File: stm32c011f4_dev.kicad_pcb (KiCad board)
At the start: 2 copper layers, 38.5 x 32 mm, 25 parts, among them J3 Conn_01x14_Pin, J5 Conn_01x14_Pin, P1 USB_C_Plug_USB2.0, SW3 SW_Push, SW4 SW_Push, U2 STM32G030K6Tx, U3 DI78L3.3UAB-DIO, Y1 LFXTAL069528CUTT

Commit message: Silkscreen update
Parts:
- moved REF** 18.5 mm to (53.5, 44.0)
- moved C3 0.50 mm to (32.0, 28.5)
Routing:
- net Earth: track 85.1 -> 98.2 mm, vias 10 -> 11
- net PB0: track 26.9 -> 27.6 mm
- net Net-(D3-A): track 9.56 -> 8.98 mm
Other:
- board text added: "3v3"
- board text added: "GND"
- board text added: "PA0"
- board text added: "PA1"
- board text added: "PA11"
- board text added: "PA12"
- board text added: "PA13"
- board text added: "PA15"
- board text added: "PA2"
- board text added: "PA3"
- board text added: "PA4"
- board text added: "PA5"
- board text added: "PA6"
- board text added: "PA7"
- board text added: "PA8"
- board text added: "PB0"
- board text added: "PB1"
- board text added: "PB2"
- board text added: "PB3"
- board text added: "PB4"
- board text added: "PB5"
- board text added: "PB6"
- board text added: "PB7"
- board text added: "PB8"
- board text added: "PB9"
- board text added: "PC6"
- board text added: "VIN"

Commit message: pcb update
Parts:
- moved SW4 0.10 mm to (24.0, 45.5)
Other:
- board size 38.5 x 32 mm -> 39 x 32 mm
- board text added: "RX"
- board text added: "TX"
- board text removed: "${REFERENCE}"
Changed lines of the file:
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@@
 	(footprint "Button_Switch_SMD:SW_SPST_EVQQ2"
 		(layer "F.Cu")
-		(at 23.9 45.5)
+		(at 24 45.5)
 		(descr "Light Touch Switch, https://industrial.panasonic.com/cdbs/www-data/pdf/ATK0000/ATK0000CE28.pdf")
 		(property "Reference" "SW4"
@@
 		(tags "LED")
 		(property "Reference" "D1"
-			(at 0 -1.43 180)
+			(at 2.2125 0 180)
 			(layer "F.SilkS")
 			(effects
@@
 		(tags "Through hole pin header THT 1x14 2.54mm single row")
 		(property "Reference" "J5"
-			(at 0 -2.33 -90)
+			(at 2 -0.84 180)
 			(layer "F.SilkS")
 			(effects
@@
 		(tags "Through hole pin header THT 1x14 2.54mm single row")
 		(property "Reference" "J3"
-			(at 0 -2.33 -90)
+			(at -2 -0.96 180)
 			(layer "F.SilkS")
 			(effects
@@
 		(tags "resistor")
 		(property "Reference" "R8"
-			(at 0 -1.43 0)
+			(at 1.7875 -1.35625 0)
 			(layer "F.SilkS")
+			(hide yes)
 			(effects
 				(font
@@
 		(tags "SMD SMT crystal")
 		(property "Reference" "Y1"
-			(at 0 -2 180)
+			(at 1.1 -2.3 180)
 			(layer "F.SilkS")
 			(effects
@@
 	)
 	(gr_rect
-		(start 18.5 20.5)
+		(start 18 20.5)
 		(end 57 52.5)
 		(stroke
@@
 		)
 	)
-	(gr_text "made by Lorbasta"
-		(at 56.5 41 90)
+	(gr_text "RX"
+		(at 46 49 0)
+		(layer "F.SilkS")
+		(effects
+			(font
+				(size 1 1)
+				(thickness 0.25)
+				(bold yes)
+			)
+			(justify left bottom)
+		)
+	)
+	(gr_text "TX"
+		(at 46 45.5 0)
 		(layer "F.SilkS")
 		(effects
@@
 		)
 	)
-	(gr_text "${REFERENCE}"
-		(at 33 38 0)
-		(layer "F.Fab")
+	(gr_text "made by Lorbasta"
+		(at 56.5 41 90)
+		(layer "F.SilkS")
 		(effects
 			(font
-				(size 0.4 0.4)
-				(thickness 0.06)
+				(size 1 1)
+				(thickness 0.25)
+				(bold yes)
 			)
+			(justify left bottom)
 		)
 	)

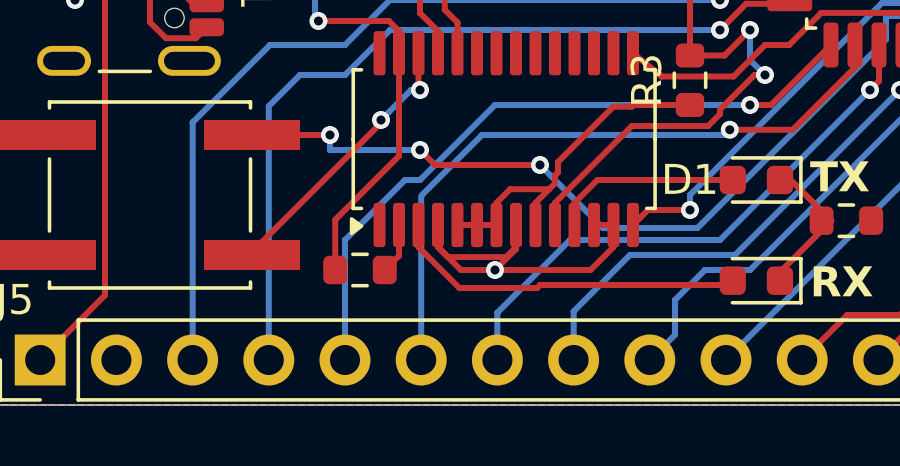
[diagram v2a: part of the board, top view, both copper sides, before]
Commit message: pcb update
fixed gnd mistakes
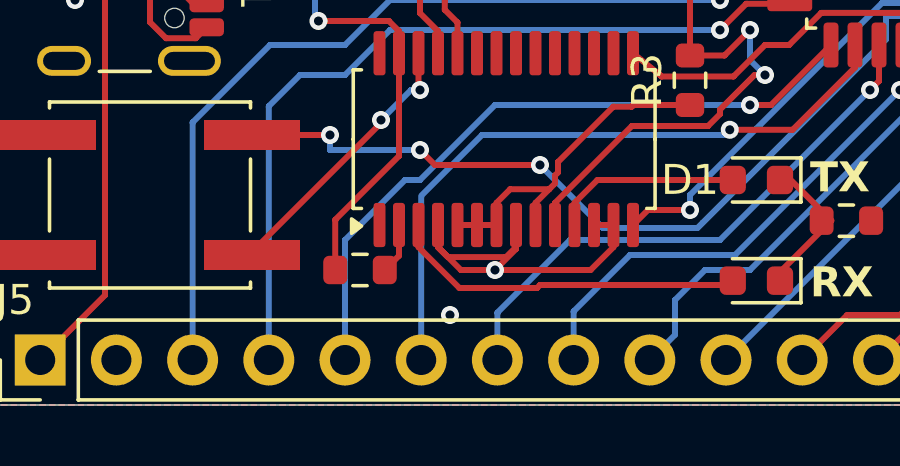
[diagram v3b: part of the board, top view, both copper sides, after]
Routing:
- net Earth: vias 11 -> 12
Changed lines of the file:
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@@
 			(layer "F.Fab")
 		)
-		(fp_text user "${REFERENCE}"
-			(at -12.5125 -15.35625 0)
-			(layer "F.Fab")
-			(effects
-				(font
-					(size 1 1)
-					(thickness 0.15)
-				)
-			)
-		)
 		(pad "1" smd roundrect
 			(at -1.65 0 180)
@@
 		(size 0.6)
 		(drill 0.3)
+		(layers "F.Cu" "B.Cu")
+		(free yes)
+		(net 2)
+	)
+	(via
+		(at 34 49.5)
+		(size 0.6)
+		(drill 0.3)

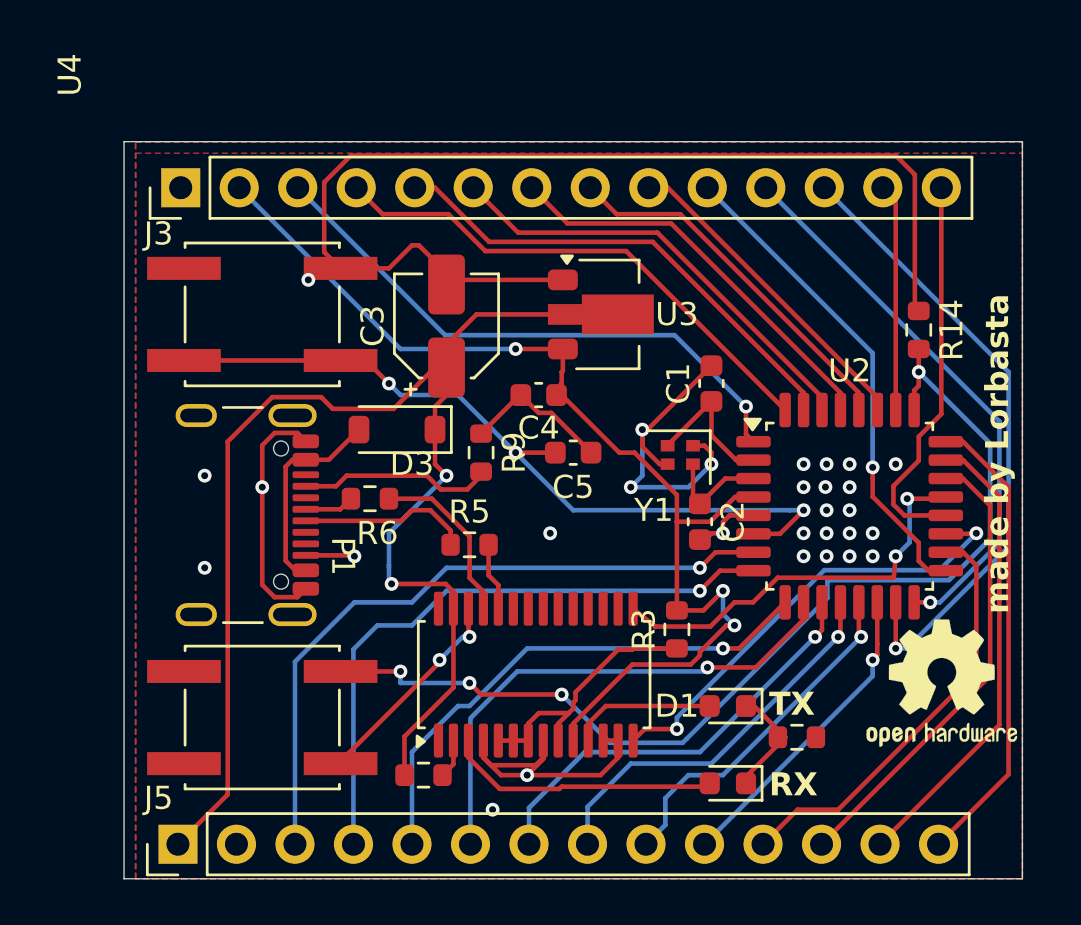
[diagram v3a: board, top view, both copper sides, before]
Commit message: PCB update
adding swd and improving traces
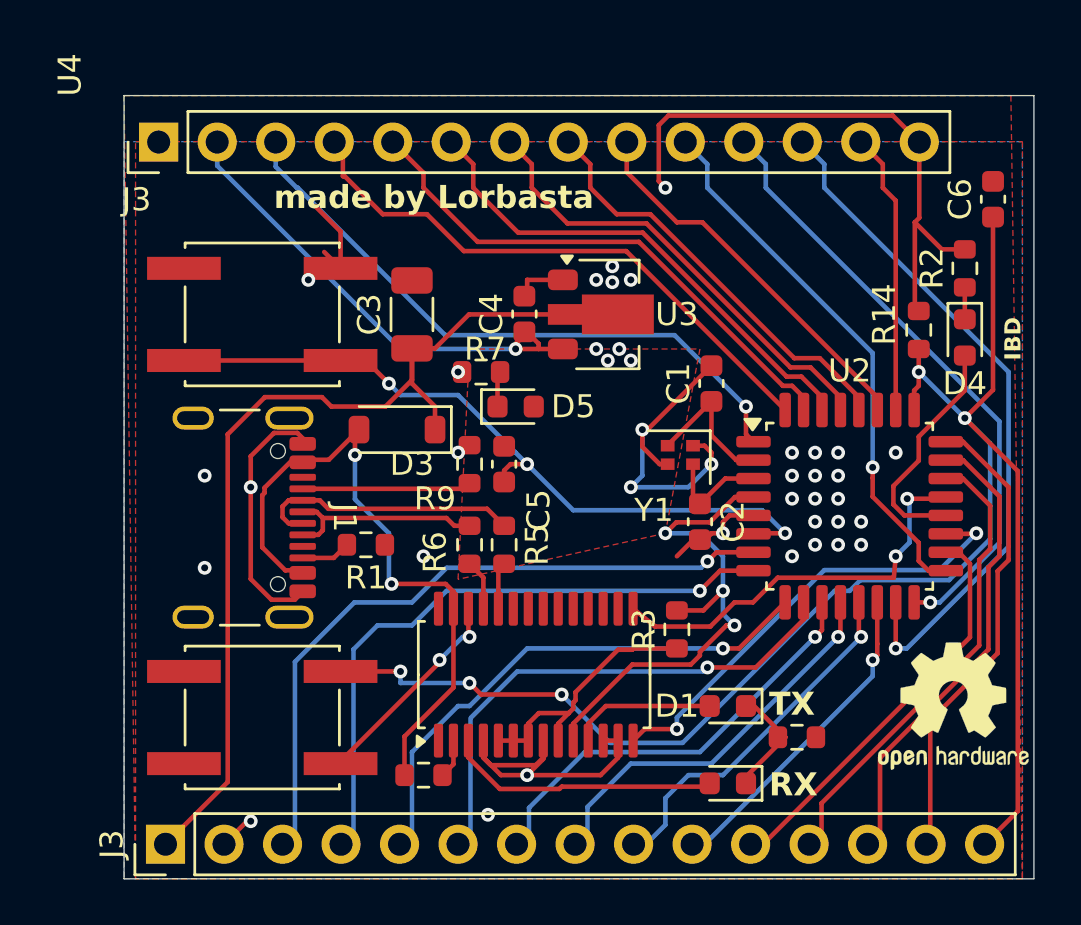
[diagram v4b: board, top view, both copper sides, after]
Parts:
- removed J5: Conn_01x14_Pin, Connector_PinHeader_2.54mm:PinHeader_1x14_P2.54mm_Vertical
- removed P1: USB_C_Plug_USB2.0, Connector_USB:USB_C_Receptacle_GCT_USB4105-xx-A_16P_TopMnt_Horizontal
- added C6: 100nF, Capacitor_SMD:C_0603_1608Metric, F.Cu at (55.7, 23.0)
- added D4: LED, LED_SMD:LED_0603_1608Metric, F.Cu at (54.5, 29.0)
- added D5: LED, LED_SMD:LED_0603_1608Metric, F.Cu at (35.0, 32.0)
- added J1: USB_C_Receptacle_USB2.0_16P, Connector_USB:USB_C_Receptacle_GCT_USB4105-xx-A_16P_TopMnt_Horizontal, F.Cu at (22.1, 36.8)
- added J3: Conn_01x15_Pin, Connector_PinHeader_2.54mm:PinHeader_1x15_P2.54mm_Vertical, F.Cu at (19.8, 51.0)
- added R1: 5k, Resistor_SMD:R_0603_1608Metric, F.Cu at (28.5, 38.0)
- added R2: 220, Resistor_SMD:R_0603_1608Metric, F.Cu at (54.5, 26.0)
- added R7: 220, Resistor_SMD:R_0603_1608Metric, F.Cu at (33.5, 30.5)
- C3: value 1uF -> 10uF; footprint Capacitor_SMD:CP_Elec_4x5.3 -> Capacitor_SMD:C_1206_3216Metric
- R9: value 56k -> 5k
- moved R6 4.77 mm to (33.0, 38.0), turned to -90 degrees
- moved C4 3.57 mm to (35.4, 28.0), turned to 90 degrees
- moved C5 3.04 mm to (34.5, 34.5), turned to 90 degrees
- moved J3 2.20 mm to (19.5, 20.5)
- moved C3 1.58 mm to (30.5, 28.0)
- moved R5 1.50 mm to (34.5, 38.0), turned to -90 degrees
- moved REF** 1.12 mm to (54.0, 45.0)
- moved R9 0.71 mm to (33.0, 34.5)
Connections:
- C3 pad 1: VBUS -> VIN
- D3 pad 1: VBUS -> VIN
- D3 pad 2: Net-(D3-A) -> VBUS
- J3 pad 14: PC6 -> Earth
- U2 pad 20: PC6 -> Net-(D4-A)
- U3 pad 2: VBUS -> VIN
- Y1 pad 2: OSC_IN -> Earth
- Y1 pad 4: Earth -> OSC_OUT
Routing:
- net VIN: track 0.00 -> 40.3 mm
- net VBUS: track 58.8 -> 28.9 mm
- net Net-(J3-Pin_15): track 44.9 -> 73.8 mm, vias 4 -> 5
- net Earth: track 98.2 -> 77.6 mm, vias 12 -> 40
- net PC6: track 17.1 -> 0.00 mm
- net Net-(D4-A): track 0.00 -> 10.2 mm
- net Net-(D3-A): track 8.98 -> 0.00 mm
- net DP: track 2.15 -> 8.99 mm
- net Net-(U4-DP): track 7.56 -> 2.20 mm
- net 3v3: track 49.2 -> 43.9 mm, vias 3 -> 4
- net DM: track 7.71 -> 11.6 mm
- net PB3: track 14.2 -> 16.8 mm
- net PB8: track 22.6 -> 25.0 mm
- net PB9: track 25.1 -> 27.5 mm
- net PB6: track 19.5 -> 21.8 mm
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- added copper zone on F.Cu, net 3v3
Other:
- board size 39 x 32 mm -> 39.5 x 34 mm
- board text added: "CLK"
- board text added: "IBD"
- board text removed: "PC6"

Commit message: Changing usb-c from smt to tht
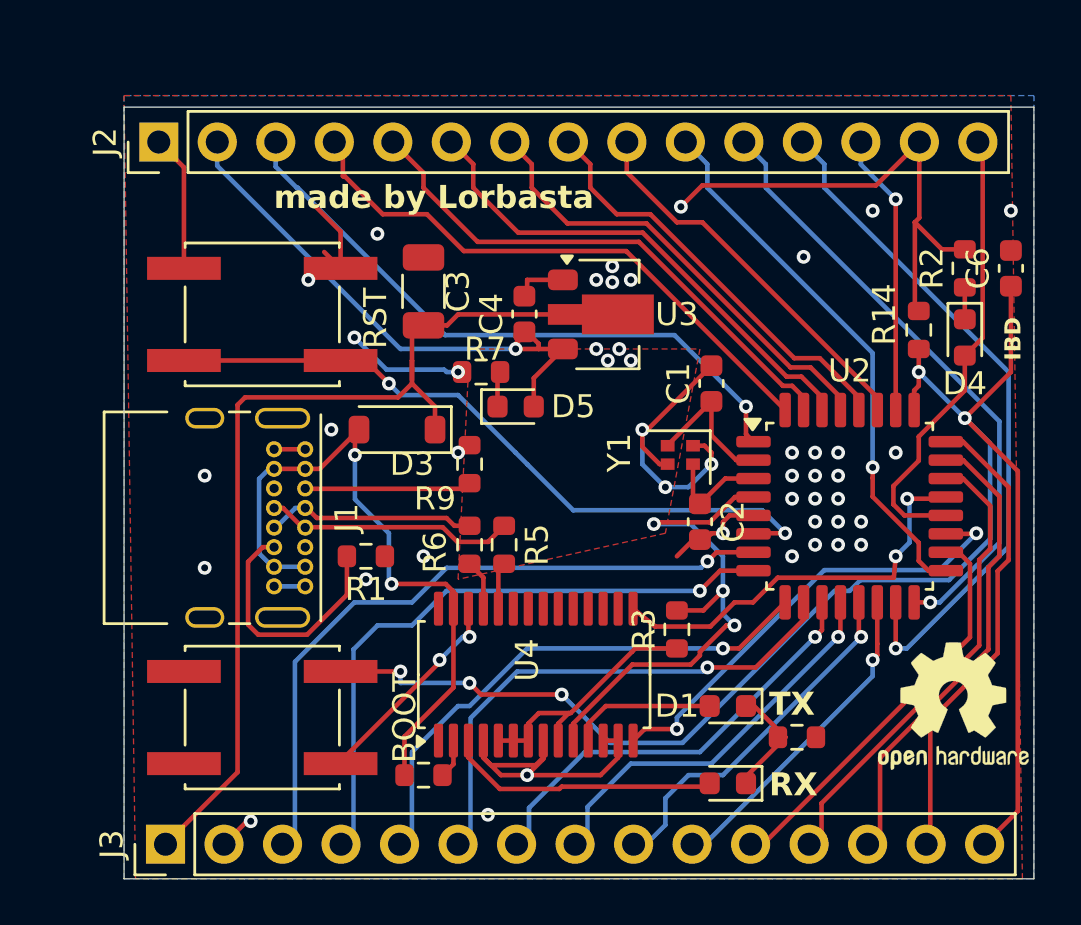
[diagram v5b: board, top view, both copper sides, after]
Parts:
- removed C5: 100nF, Capacitor_SMD:C_0603_1608Metric
- removed the J3 at (19.5, 20.5)
- added J2: Conn_01x15_Pin, Connector_PinHeader_2.54mm:PinHeader_1x15_P2.54mm_Vertical, F.Cu at (19.5, 20.5)
- J1: footprint Connector_USB:USB_C_Receptacle_GCT_USB4105-xx-A_16P_TopMnt_Horizontal -> Connector_USB:USB_C_Receptacle_GCT_USB4085
- moved J1 4.81 mm to (25.9, 33.9)
- moved C6 3.10 mm to (56.5, 26.0)
- moved C3 1.12 mm to (31.0, 27.0)
- moved R1 0.50 mm to (28.5, 38.5)
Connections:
- net Net-(D4-A) renamed PC6
- Y1 pad 2: Earth -> OSC_IN
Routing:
- net PC6: track 10.2 -> 20.3 mm
- net Net-(J1-CC2): track 2.16 -> 11.0 mm
- net 3v3: track 43.9 -> 47.9 mm
- net Net-(J3-Pin_15): track 73.8 -> 71.1 mm
- net Net-(U2-NRST): track 32.2 -> 30.6 mm, vias 3 -> 2
- net Earth: track 77.6 -> 76.7 mm, vias 40 -> 46
- net DM: track 11.6 -> 10.9 mm
- net VBUS: track 28.9 -> 29.6 mm
- net PA15: vias 0 -> 1
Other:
- board size 39.5 x 34 mm -> 39.5 x 33.5 mm
- board text added: "BOOT"
- board text added: "RST"

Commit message: tht usb and one resistor per led cathode
:333
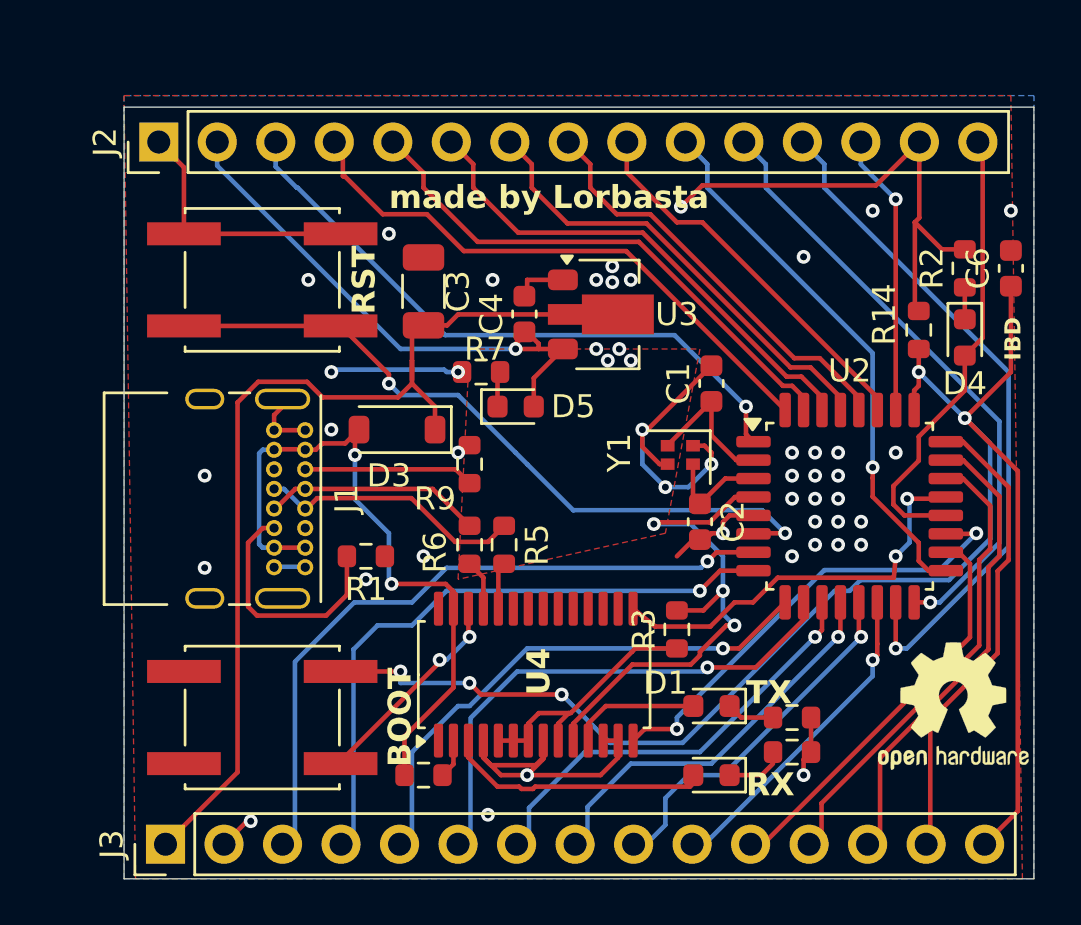
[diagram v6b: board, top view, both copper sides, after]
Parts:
- added R10: 220, Resistor_SMD:R_0603_1608Metric, F.Cu at (47.0, 45.5)
- moved SW3 1.50 mm to (24.0, 26.5)
- moved J1 0.83 mm to (25.9, 33.0)
- moved D2 0.80 mm to (43.5, 48.0)
- moved D1 0.71 mm to (43.5, 45.0)
- moved R8 0.68 mm to (47.0, 47.0)
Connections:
- D2 pad 1: Net-(D1-K) -> Net-(D2-K)
- R8 pad 1: Net-(D1-K) -> Net-(D2-K)
- Y1 pad 2: OSC_IN -> Earth
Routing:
- net Earth: track 76.7 -> 81.4 mm, vias 46 -> 48
- net Net-(D1-K): track 5.13 -> 2.09 mm
- net Net-(D2-K): track 0.00 -> 2.09 mm
- net Net-(D2-A): track 12.2 -> 11.2 mm
- net DM: track 10.9 -> 11.9 mm
- net Net-(U2-NRST): track 30.6 -> 31.4 mm
- net Net-(D1-A): track 6.33 -> 5.62 mm
- net VIN: track 40.7 -> 41.3 mm
